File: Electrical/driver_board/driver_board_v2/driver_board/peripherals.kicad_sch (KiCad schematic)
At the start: 3 parts, among them SW3 SW_Push, SW4 SW_Push, SW5 SW_Push

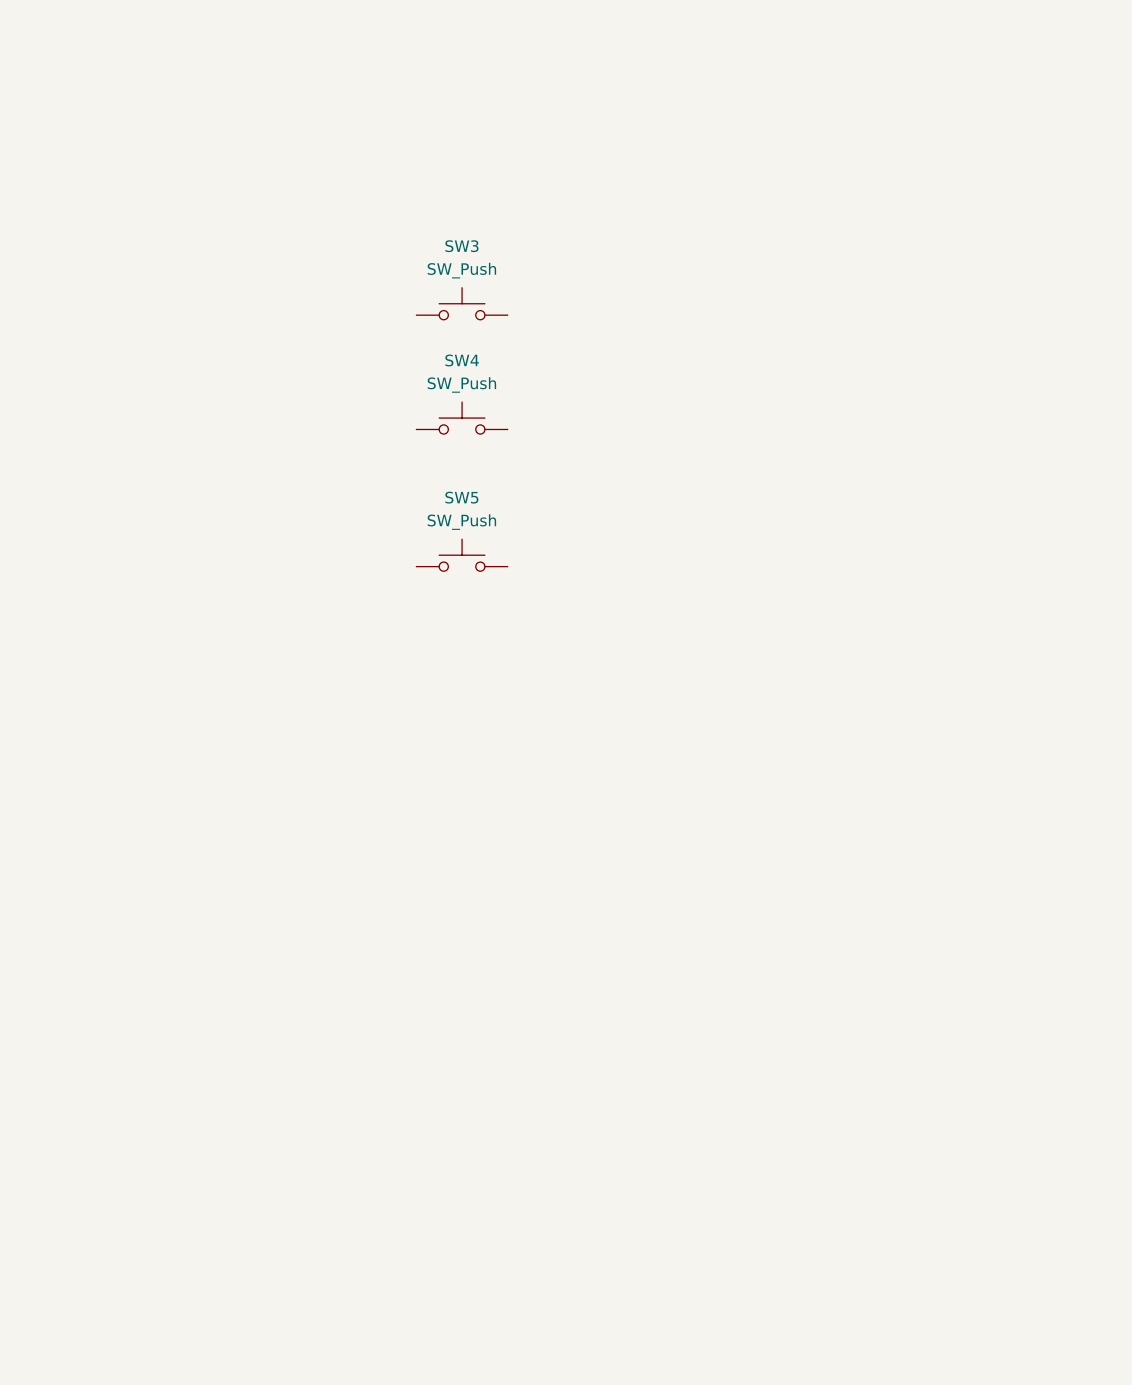
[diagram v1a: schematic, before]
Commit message: Changed switches to encoder
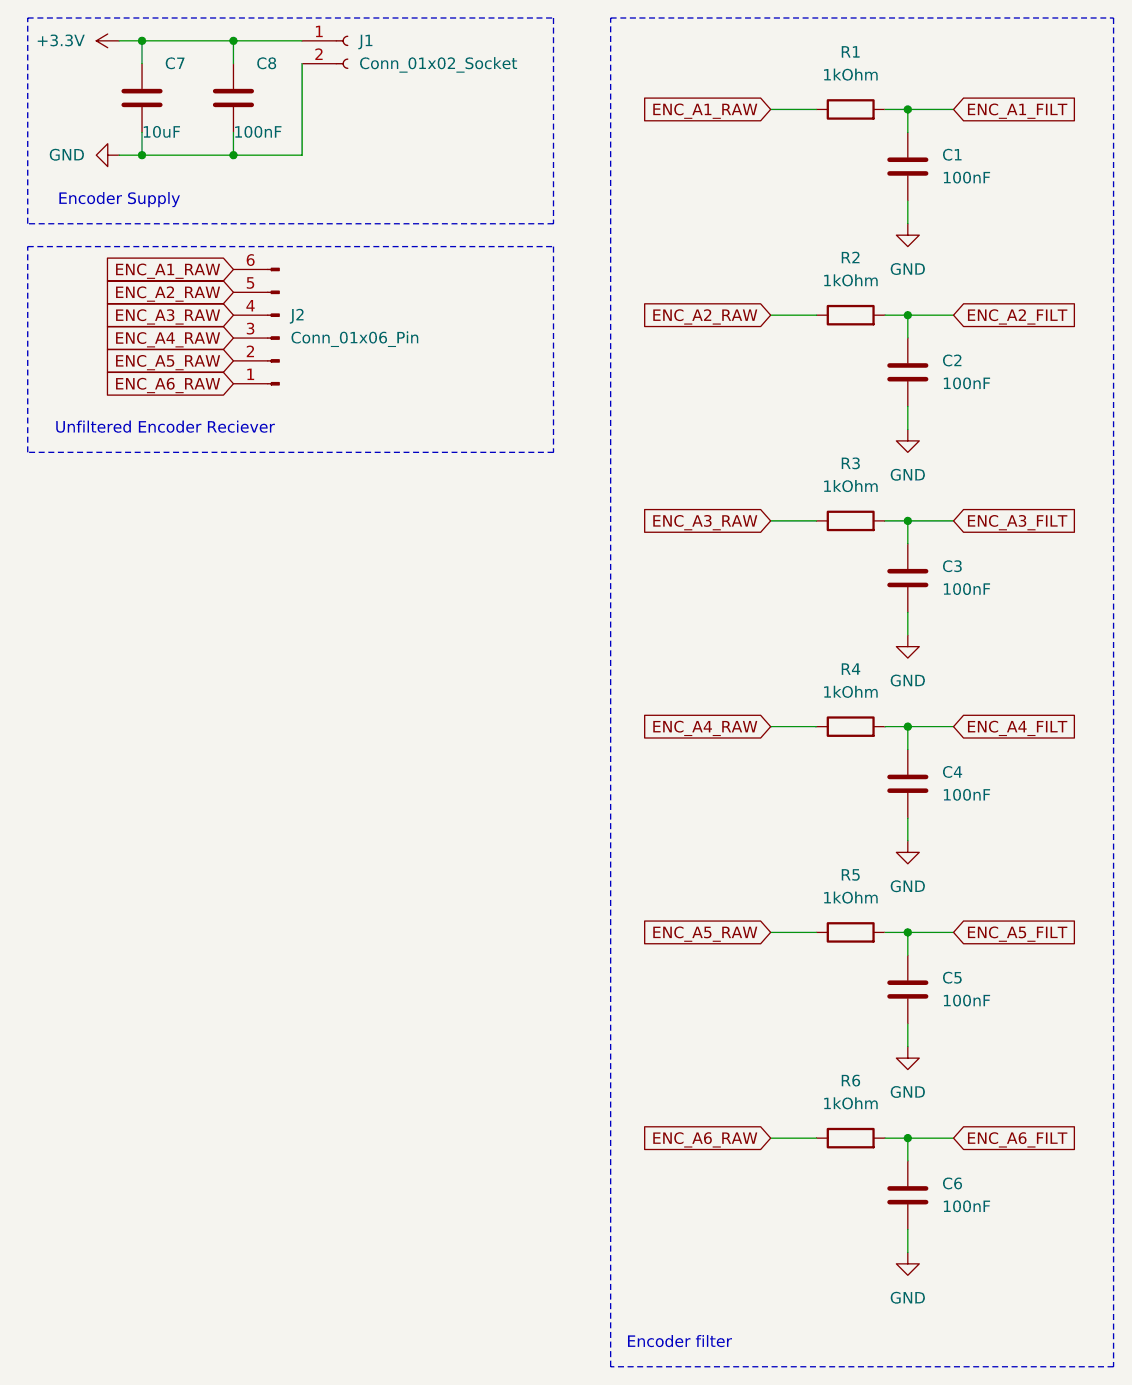
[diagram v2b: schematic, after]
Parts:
- removed SW3, SW4, SW5: SW_Push, symbol Switch:SW_Push
- added C1, C2, C3, C4, C5, C6, C8: 100nF, symbol Device:C
- added C7: 10uF, symbol Device:C
- added J1: Conn_01x02_Socket, symbol Connector:Conn_01x02_Socket
- added J2: Conn_01x06_Pin, symbol Connector:Conn_01x06_Pin
- added R1, R2, R3, R4, R5, R6: 1kOhm, symbol Device:R
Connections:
- new net +3.3V: C7.1, C8.1, J1.1 (Pin_1)
- new net ENC_A1_FILT: C1.1, R1.2
- new net ENC_A1_RAW: J2.6 (Pin_6), R1.1
- new net ENC_A2_FILT: C2.1, R2.2
- new net ENC_A2_RAW: J2.5 (Pin_5), R2.1
- new net ENC_A3_FILT: C3.1, R3.2
- new net ENC_A3_RAW: J2.4 (Pin_4), R3.1
- new net ENC_A4_FILT: C4.1, R4.2
- new net ENC_A4_RAW: J2.3 (Pin_3), R4.1
- new net ENC_A5_FILT: C5.1, R5.2
- new net ENC_A5_RAW: J2.2 (Pin_2), R5.1
- new net ENC_A6_FILT: C6.1, R6.2
- new net ENC_A6_RAW: J2.1 (Pin_1), R6.1
- new net GND: C1.2, C2.2, C3.2, C4.2, C5.2, C6.2, C7.2, C8.2, J1.2 (Pin_2)
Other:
- note added: "Encoder Supply"
- note added: "Encoder filter"
- note added: "Unfiltered Encoder Reciever"

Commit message: Added gripper
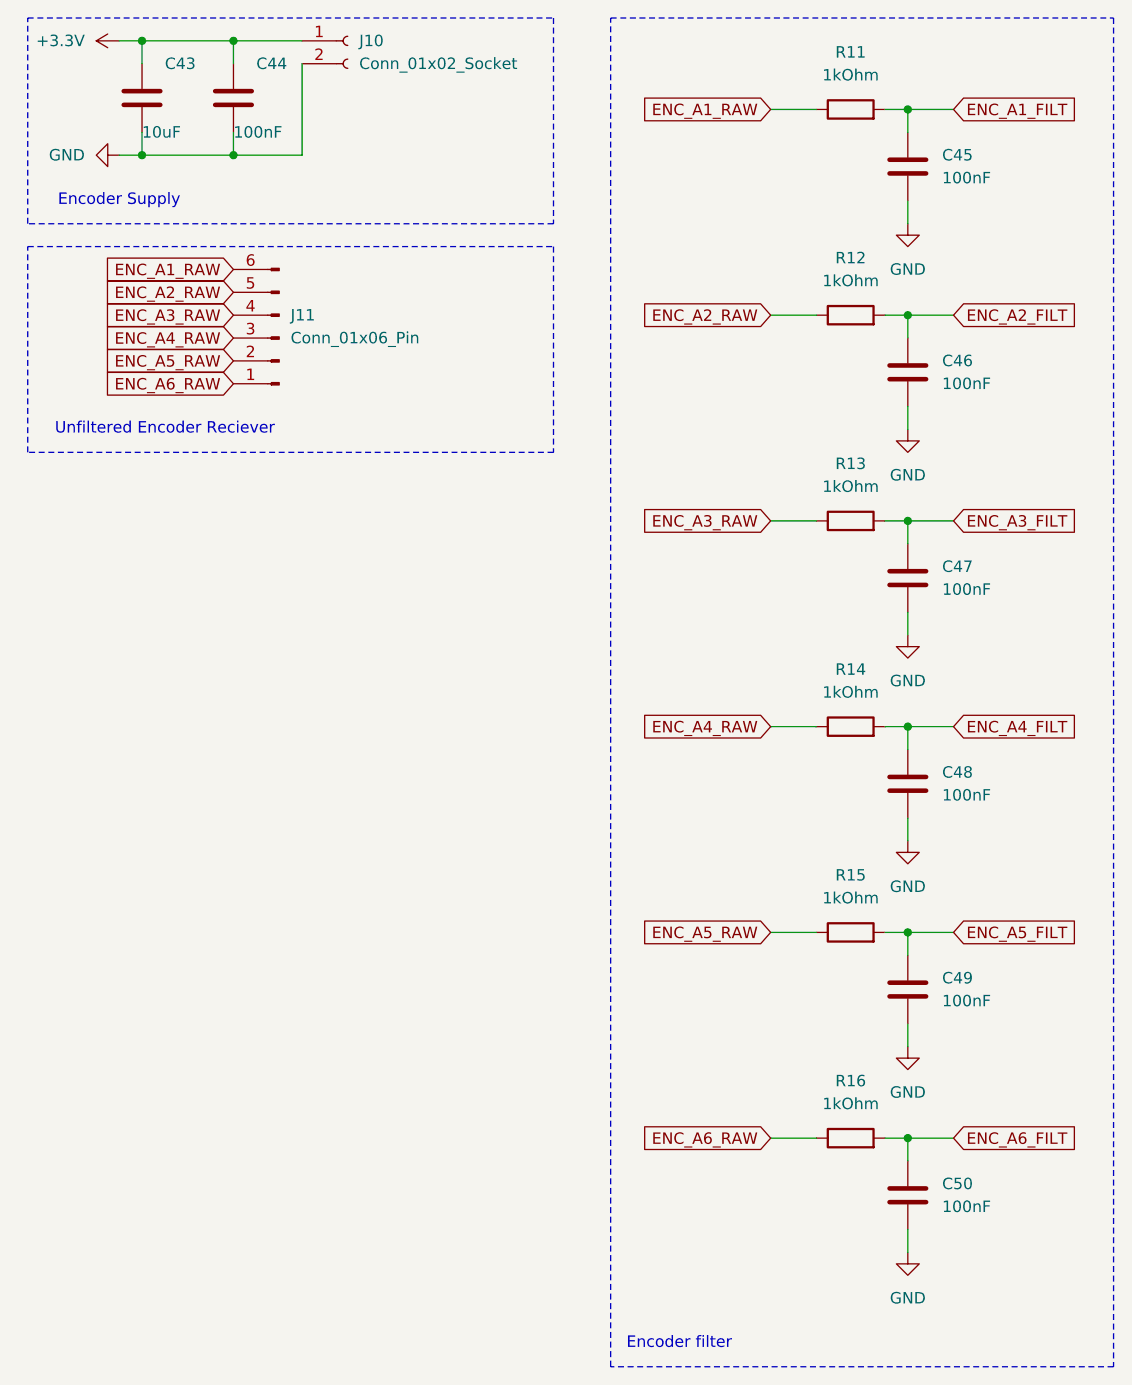
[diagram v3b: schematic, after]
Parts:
- renumbered C7 to C43, C8 to C44, C1 to C45, C2 to C46, C3 to C47, C4 to C48, C5 to C49, C6 to C50, J1 to J10, J2 to J11, R1 to R11, R2 to R12, R3 to R13, R4 to R14, R5 to R15, R6 to R16
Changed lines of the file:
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@@
 		(dnp no)
 		(fields_autoplaced yes)
-		(property "Reference" "R5"
+		(property "Reference" "R15"
 			(at 132.08 125.73 90)
 			(effects
@@
 				)
 			)
+			(project "driver_board"
+				(path "/914a9dfd-cc72-459d-a4b5-1249c31e6215/1d053789-bb06-47b5-b093-e7b74b4d3277"
+					(reference "R15")
+					(unit 1)
+				)
+			)
 		)
 	)
@@
 		(dnp no)
 		(fields_autoplaced yes)
-		(property "Reference" "C3"
+		(property "Reference" "C47"
 			(at 142.24 91.4399 0)
 			(effects
@@
 				)
 			)
+			(project "driver_board"
+				(path "/914a9dfd-cc72-459d-a4b5-1249c31e6215/1d053789-bb06-47b5-b093-e7b74b4d3277"
+					(reference "C47")
+					(unit 1)
+				)
+			)
 		)
 	)
@@
 		(dnp no)
 		(fields_autoplaced yes)
-		(property "Reference" "C5"
+		(property "Reference" "C49"
 			(at 142.24 137.1599 0)
 			(effects
@@
 				)
 			)
+			(project "driver_board"
+				(path "/914a9dfd-cc72-459d-a4b5-1249c31e6215/1d053789-bb06-47b5-b093-e7b74b4d3277"
+					(reference "C49")
+					(unit 1)
+				)
+			)
 		)
 	)
@@
 		(on_board yes)
 		(dnp no)
-		(property "Reference" "C8"
+		(property "Reference" "C44"
 			(at 66.04 35.56 0)
 			(effects
@@
 				)
 			)
+			(project "driver_board"
+				(path "/914a9dfd-cc72-459d-a4b5-1249c31e6215/1d053789-bb06-47b5-b093-e7b74b4d3277"
+					(reference "C44")
+					(unit 1)
+				)
+			)
 		)
 	)
@@
 		(dnp no)
 		(fields_autoplaced yes)
-		(property "Reference" "#PWR01"
+		(property "Reference" "#PWR060"
 			(at 54.61 33.02 0)
 			(effects
@@
 				)
 			)
+			(project "driver_board"
+				(path "/914a9dfd-cc72-459d-a4b5-1249c31e6215/1d053789-bb06-47b5-b093-e7b74b4d3277"
+					(reference "#PWR060")
+					(unit 1)
+				)
+			)
 		)
 	)
@@
 		(dnp no)
 		(fields_autoplaced yes)
-		(property "Reference" "R6"
+		(property "Reference" "R16"
 			(at 132.08 148.59 90)
 			(effects
@@
 				)
 			)
+			(project "driver_board"
+				(path "/914a9dfd-cc72-459d-a4b5-1249c31e6215/1d053789-bb06-47b5-b093-e7b74b4d3277"
+					(reference "R16")
+					(unit 1)
+				)
+			)
 		)
 	)
@@
 		(dnp no)
 		(fields_autoplaced yes)
-		(property "Reference" "R3"
+		(property "Reference" "R13"
 			(at 132.08 80.01 90)
 			(effects
@@
 				)
 			)
+			(project "driver_board"
+				(path "/914a9dfd-cc72-459d-a4b5-1249c31e6215/1d053789-bb06-47b5-b093-e7b74b4d3277"
+					(reference "R13")
+					(unit 1)
+				)
+			)
 		)
 	)
@@
 		(on_board yes)
 		(dnp no)
-		(property "Reference" "C7"
+		(property "Reference" "C43"
 			(at 55.88 35.56 0)
 			(effects
@@
 				)
 			)
+			(project "driver_board"
+				(path "/914a9dfd-cc72-459d-a4b5-1249c31e6215/1d053789-bb06-47b5-b093-e7b74b4d3277"
+					(reference "C43")
+					(unit 1)
+				)
+			)
 		)
 	)
@@
 		(dnp no)
 		(fields_autoplaced yes)
-		(property "Reference" "#PWR08"
+		(property "Reference" "#PWR067"
 			(at 138.43 173.99 0)
 			(effects
@@
 				)
 			)
+			(project "driver_board"
+				(path "/914a9dfd-cc72-459d-a4b5-1249c31e6215/1d053789-bb06-47b5-b093-e7b74b4d3277"
+					(reference "#PWR067")
+					(unit 1)
+				)
+			)
 		)
 	)
@@
 		(dnp no)
 		(fields_autoplaced yes)
-		(property "Reference" "#PWR03"
+		(property "Reference" "#PWR062"
 			(at 138.43 59.69 0)
 			(effects
@@
 				)
 			)
+			(project "driver_board"
+				(path "/914a9dfd-cc72-459d-a4b5-1249c31e6215/1d053789-bb06-47b5-b093-e7b74b4d3277"
+					(reference "#PWR062")
+					(unit 1)
+				)
+			)
 		)
 	)
@@
 		(dnp no)
 		(fields_autoplaced yes)
-		(property "Reference" "R2"
+		(property "Reference" "R12"
 			(at 132.08 57.15 90)
 			(effects
@@
 				)
 			)
+			(project "driver_board"
+				(path "/914a9dfd-cc72-459d-a4b5-1249c31e6215/1d053789-bb06-47b5-b093-e7b74b4d3277"
+					(reference "R12")
+					(unit 1)
+				)
+			)
 		)
 	)
@@
 		(dnp no)
 		(fields_autoplaced yes)
-		(property "Reference" "#PWR06"
+		(property "Reference" "#PWR065"
 			(at 138.43 128.27 0)
 			(effects
@@
 				)
 			)
+			(project "driver_board"
+				(path "/914a9dfd-cc72-459d-a4b5-1249c31e6215/1d053789-bb06-47b5-b093-e7b74b4d3277"
+					(reference "#PWR065")
+					(unit 1)
+				)
+			)
 		)
 	)
@@
 		(dnp no)
 		(fields_autoplaced yes)
-		(property "Reference" "R1"
+		(property "Reference" "R11"
 			(at 132.08 34.29 90)
 			(effects
@@
 				)
 			)
+			(project "driver_board"
+				(path "/914a9dfd-cc72-459d-a4b5-1249c31e6215/1d053789-bb06-47b5-b093-e7b74b4d3277"
+					(reference "R11")
+					(unit 1)
+				)
+			)
 		)
 	)
@@
 		(dnp no)
 		(fields_autoplaced yes)
-		(property "Reference" "#PWR05"
+		(property "Reference" "#PWR064"
 			(at 138.43 105.41 0)
 			(effects
@@
 				)
 			)
+			(project "driver_board"
+				(path "/914a9dfd-cc72-459d-a4b5-1249c31e6215/1d053789-bb06-47b5-b093-e7b74b4d3277"
+					(reference "#PWR064")
+					(unit 1)
+				)
+			)
 		)
 	)
@@
 		(dnp no)
 		(fields_autoplaced yes)
-		(property "Reference" "#PWR07"
+		(property "Reference" "#PWR066"
 			(at 138.43 151.13 0)
 			(effects
@@
 				)
 			)
+			(project "driver_board"
+				(path "/914a9dfd-cc72-459d-a4b5-1249c31e6215/1d053789-bb06-47b5-b093-e7b74b4d3277"
+					(reference "#PWR066")
+					(unit 1)
+				)
+			)
 		)
 	)
@@
 		(dnp no)
 		(fields_autoplaced yes)
-		(property "Reference" "C4"
+		(property "Reference" "C48"
 			(at 142.24 114.2999 0)
 			(effects
@@
 				)
 			)
+			(project "driver_board"
+				(path "/914a9dfd-cc72-459d-a4b5-1249c31e6215/1d053789-bb06-47b5-b093-e7b74b4d3277"
+					(reference "C48")
+					(unit 1)
+				)
+			)
 		)
 	)
@@
 		(dnp no)
 		(fields_autoplaced yes)
-		(property "Reference" "J2"
+		(property "Reference" "J11"
 			(at 69.85 63.4999 0)
 			(effects
@@
 				)
 			)
+			(project "driver_board"
+				(path "/914a9dfd-cc72-459d-a4b5-1249c31e6215/1d053789-bb06-47b5-b093-e7b74b4d3277"
+					(reference "J11")
+					(unit 1)
+				)
+			)
 		)
 	)
@@
 		(dnp no)
 		(fields_autoplaced yes)
-		(property "Reference" "C6"
+		(property "Reference" "C50"
 			(at 142.24 160.0199 0)
 			(effects
@@
 				)
 			)
+			(project "driver_board"
+				(path "/914a9dfd-cc72-459d-a4b5-1249c31e6215/1d053789-bb06-47b5-b093-e7b74b4d3277"
+					(reference "C50")
+					(unit 1)
+				)
+			)
 		)
 	)
@@
 		(dnp no)
 		(fields_autoplaced yes)
-		(property "Reference" "C2"
+		(property "Reference" "C46"
 			(at 142.24 68.5799 0)
 			(effects
@@
 				)
 			)
+			(project "driver_board"
+				(path "/914a9dfd-cc72-459d-a4b5-1249c31e6215/1d053789-bb06-47b5-b093-e7b74b4d3277"
+					(reference "C46")
+					(unit 1)
+				)
+			)
 		)
 	)
@@
 		(dnp no)
 		(fields_autoplaced yes)
-		(property "Reference" "C1"
+		(property "Reference" "C45"
 			(at 142.24 45.7199 0)
 			(effects
@@
 				)
 			)
+			(project "driver_board"
+				(path "/914a9dfd-cc72-459d-a4b5-1249c31e6215/1d053789-bb06-47b5-b093-e7b74b4d3277"
+					(reference "C45")
+					(unit 1)
+				)
+			)
 		)
 	)
@@
 		(dnp no)
 		(fields_autoplaced yes)
-		(property "Reference" "J1"
+		(property "Reference" "J10"
 			(at 77.47 33.0199 0)
 			(effects
@@
 				)
 			)
+			(project "driver_board"
+				(path "/914a9dfd-cc72-459d-a4b5-1249c31e6215/1d053789-bb06-47b5-b093-e7b74b4d3277"
+					(reference "J10")
+					(unit 1)
+				)
+			)
 		)
 	)
@@
 		(dnp no)
 		(fields_autoplaced yes)
-		(property "Reference" "#PWR02"
+		(property "Reference" "#PWR061"
 			(at 44.45 45.72 0)
 			(effects
@@
 				)
 			)
+			(project "driver_board"
+				(path "/914a9dfd-cc72-459d-a4b5-1249c31e6215/1d053789-bb06-47b5-b093-e7b74b4d3277"
+					(reference "#PWR061")
+					(unit 1)
+				)
+			)
 		)
 	)
@@
 		(dnp no)
 		(fields_autoplaced yes)
-		(property "Reference" "#PWR04"
+		(property "Reference" "#PWR063"
 			(at 138.43 82.55 0)
 			(effects
@@
 				)
 			)
+			(project "driver_board"
+				(path "/914a9dfd-cc72-459d-a4b5-1249c31e6215/1d053789-bb06-47b5-b093-e7b74b4d3277"
+					(reference "#PWR063")
+					(unit 1)
+				)
+			)
 		)
 	)
@@
 		(dnp no)
 		(fields_autoplaced yes)
-		(property "Reference" "R4"
+		(property "Reference" "R14"
 			(at 132.08 102.87 90)
 			(effects
@@
 					(unit 1)
 				)
+			)
+			(project "driver_board"
+				(path "/914a9dfd-cc72-459d-a4b5-1249c31e6215/1d053789-bb06-47b5-b093-e7b74b4d3277"
+					(reference "R14")
+					(unit 1)
+				)
